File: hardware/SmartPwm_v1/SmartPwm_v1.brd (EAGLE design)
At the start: 154.6 x 198.1 mm, 42 parts, among them IC1 7805T, J1 ESP32-PICO-KIT, Q1 IRF3704-H, Q2 IRF3704-H, Q3 IRF3704-H, Q4 IRF3704-H, U1 ICL7667CBAZA, U3 ICL7667CBAZA

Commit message: remove 1 knob, add 3 individual leds, start component placment
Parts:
- removed MT5: PEC11R-4215F-S0024, PEC11R-4215F-S0024:XDCR_PEC11R-4215F-S0024
- moved SV4 410.4 mm to (96.5, 53.3), turned to 90 degrees
- moved SV3 401.5 mm to (90.2, 53.3), turned to 90 degrees
- moved SV5 387.5 mm to (88.9, 21.6), turned to 90 degrees
- moved C1 359.8 mm to (74.9, 11.4)
- moved U$6 357.4 mm to (77.5, 30.5), turned to 90 degrees
- moved U$8 341.5 mm to (66.0, 5.08)
- moved U3 331.6 mm to (34.3, 62.2)
- moved R8 319.9 mm to (82.5, 8.89), turned to 270 degrees
- moved R6 316.3 mm to (82.5, 12.7)
- moved R9 314.2 mm to (69.8, 11.4), turned to 180 degrees
- moved R7 313.9 mm to (78.7, 8.89), turned to 270 degrees
- moved R10 313.4 mm to (64.8, 11.4), turned to 180 degrees
- moved C10 304.5 mm to (34.3, 71.1), turned to 180 degrees
- moved C12 299.1 mm to (34.3, 67.3), turned to 180 degrees
- moved U$7 297.5 mm to (96.5, 21.6), turned to 270 degrees
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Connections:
- net LDAT3V3 renamed LDAT1_3V3
- removed net K5_A: J1.J3_9, MT5.A
- removed net K5_B: J1.J3_6, MT5.B
- removed net K5_S: J1.J2_17, MT5.2
- removed net LDAT5V: SV2.2, SV2.3, SV3.2, SV3.3, SV4.2, SV4.3, SV5.2, SV5.3, U$6.3
- new net LDAT1_5V: SV1.2, SV1.3, U$6.3
- new net LDAT2_3V3: J1.J2_7, U$6.5
- new net LDAT2_5V: SV2.2, SV2.3, U$6.6
- new net LDAT3_3V3: J1.J3_6, U$6.9
- new net LDAT3_5V: SV3.2, SV3.3, U$6.8
- new net LDAT4_3V3: J1.J3_9, U$6.12
- new net LDAT4_5V: SV4.2, SV4.3, U$6.11
- net GND: now also U$6.13, U$6.4; no longer MT5.1, MT5.COM, MT5.S1, MT5.S2, U$6.5, U$6.9
- net SCL: now also SV5.4; no longer SV1.4
- net SDA: now also SV5.3; no longer SV1.3
- net VCC: no longer U$6.12, U$6.13, U$6.4
- net VDD: now also SV1.4; no longer SV5.4
- net VEE: now also SV5.2; no longer SV1.2
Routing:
- net LOAD_RET4: track 0.00 -> 87.8 mm
- net LOAD_RET3: track 0.00 -> 63.7 mm
- net LOAD_RET2: track 0.00 -> 42.9 mm
- net SCL: track 0.00 -> 38.0 mm
- net VEE: track 0.00 -> 37.2 mm
- net SDA: track 0.00 -> 30.0 mm
- net LOAD_RET1: track 0.00 -> 18.7 mm
- net VDD: track 0.00 -> 11.7 mm
- net TDAT: track 0.00 -> 10.1 mm
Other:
- board size 154.6 x 198.1 mm -> 101.6 x 76.2 mm
- board text added: "7667"
- board text added: "G D D V"
- board text added: "G V D C"

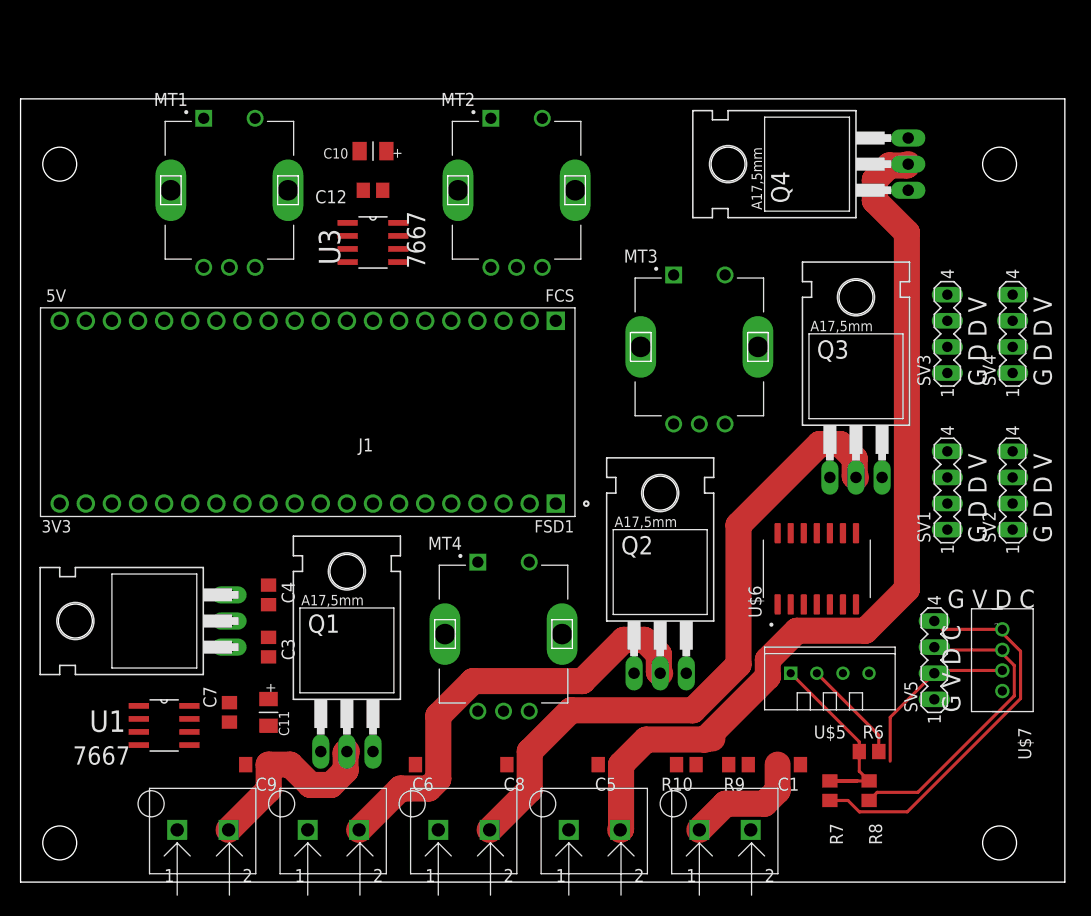
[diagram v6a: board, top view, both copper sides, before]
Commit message: redo placment for more efficient routing
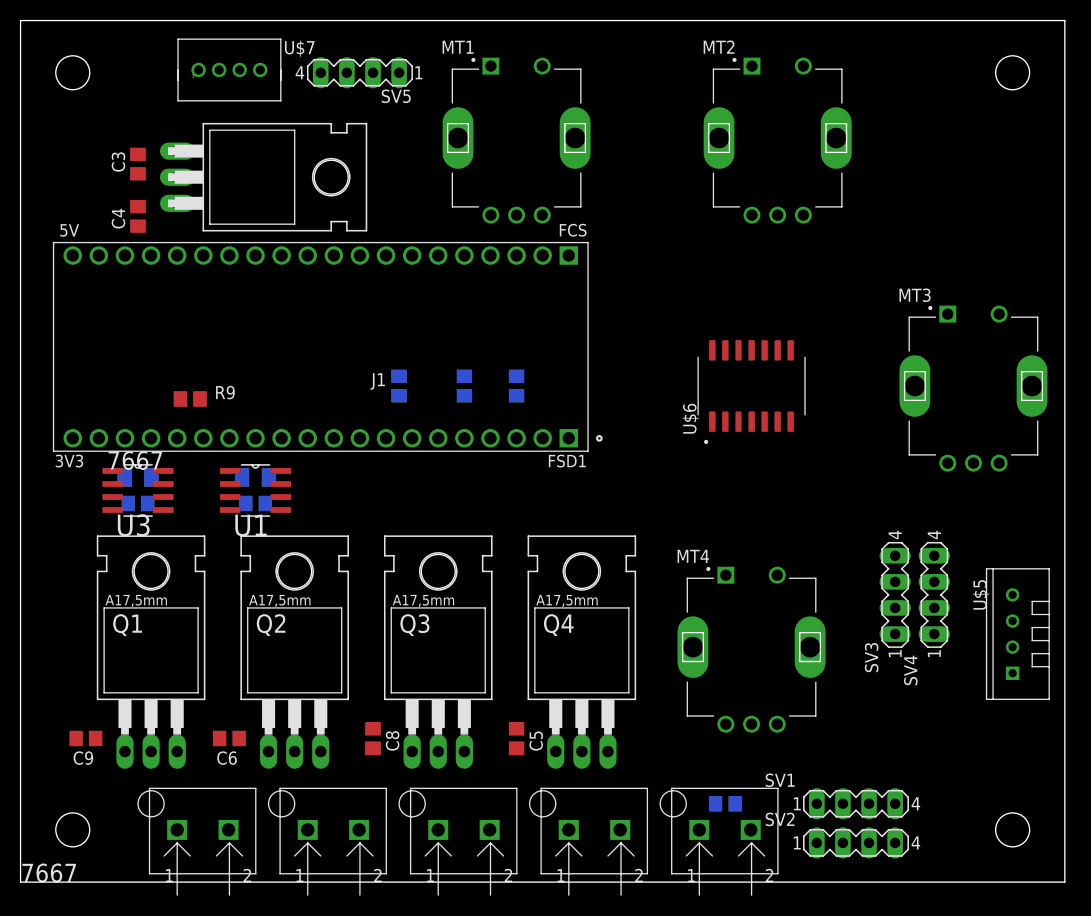
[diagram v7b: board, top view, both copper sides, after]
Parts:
- moved U$7 96.0 mm to (20.3, 80.0), turned to 0 degrees
- moved SV5 79.9 mm to (33.0, 78.7), turned to 180 degrees
- moved R9 64.1 mm to (16.5, 47.0)
- moved R10 59.9 mm to (16.5, 47.0), flipped to the bottom
- moved R6 57.9 mm to (36.8, 48.3), flipped to the bottom, turned to 270 degrees
- moved Q4 56.8 mm to (54.6, 19.1), turned to 0 degrees
- moved R7 53.1 mm to (43.2, 48.3), flipped to the bottom
- moved R8 52.2 mm to (48.3, 48.3), flipped to the bottom
- moved C3 48.7 mm to (11.4, 69.8), turned to 270 degrees
- moved Q3 48.6 mm to (40.6, 19.1)
- moved IC1 45.8 mm to (25.4, 68.6), turned to 270 degrees
- moved C4 39.0 mm to (11.4, 64.8), turned to 90 degrees
- moved SV2 37.5 mm to (81.3, 3.81), turned to 0 degrees
- moved Q2 36.4 mm to (26.7, 19.1)
- moved C10 33.7 mm to (22.9, 39.4), flipped to the bottom, turned to 0 degrees
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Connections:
- net CTRL1: now also J1.J2_17; no longer J1.J3_12
- net CTRL2: now also J1.J2_16; no longer J1.J3_13
- net CTRL3: now also J1.J2_14; no longer J1.J3_11
- net CTRL4: now also J1.J2_15; no longer J1.J3_14
- net K4_A: no longer J1.J2_14
- net K4_S: no longer J1.J2_15
- net VDIV: no longer J1.J2_16
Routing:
- net LOAD_RET4: track 87.8 -> 0.00 mm
- net LOAD_RET3: track 63.7 -> 0.00 mm
- net LOAD_RET2: track 42.9 -> 0.00 mm
- net SCL: track 38.0 -> 0.00 mm
- net VEE: track 37.2 -> 0.00 mm
- net SDA: track 30.0 -> 0.00 mm
- net LOAD_RET1: track 18.7 -> 0.00 mm
- net VDD: track 11.7 -> 0.00 mm
- net TDAT: track 10.1 -> 0.00 mm
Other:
- board size 101.6 x 76.2 mm -> 101.6 x 83.8 mm
- board text removed: "G D D V"
- board text removed: "G V D C"

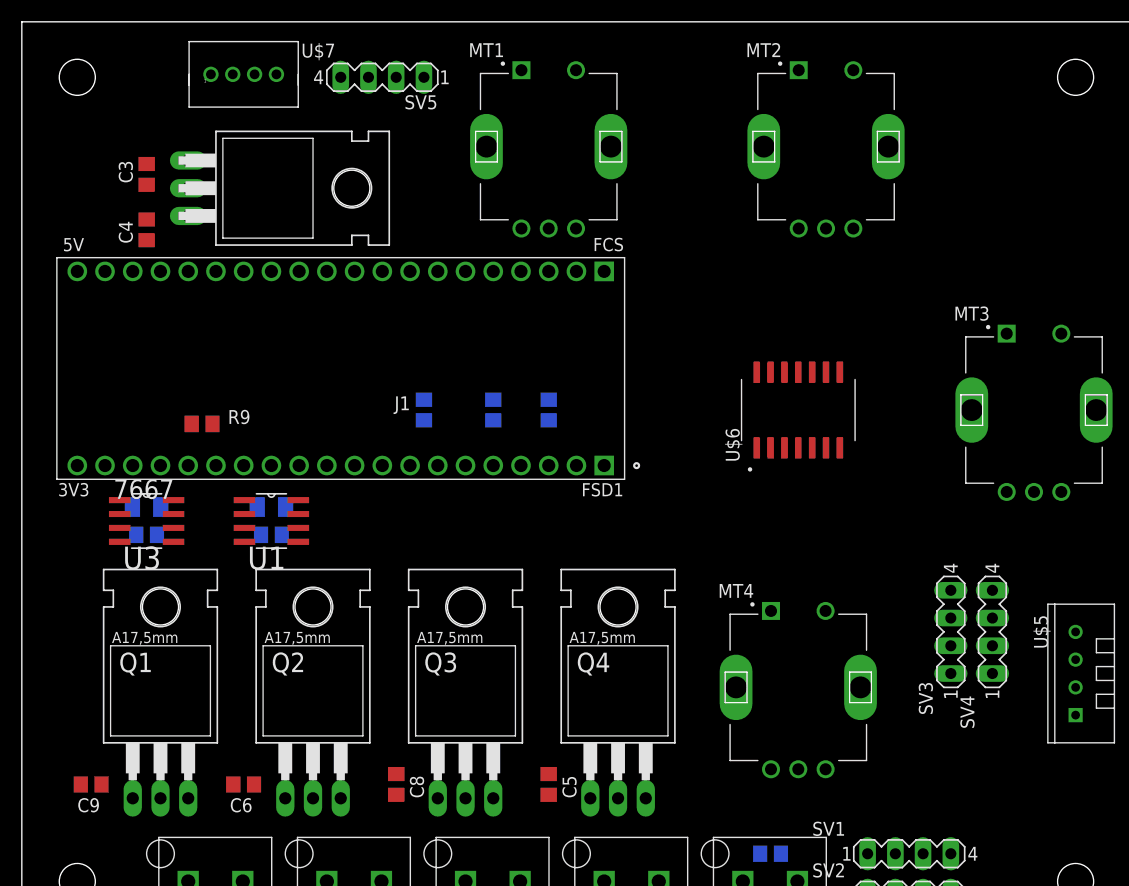
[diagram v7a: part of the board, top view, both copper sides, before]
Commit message: rewire gpios, preliminary routing
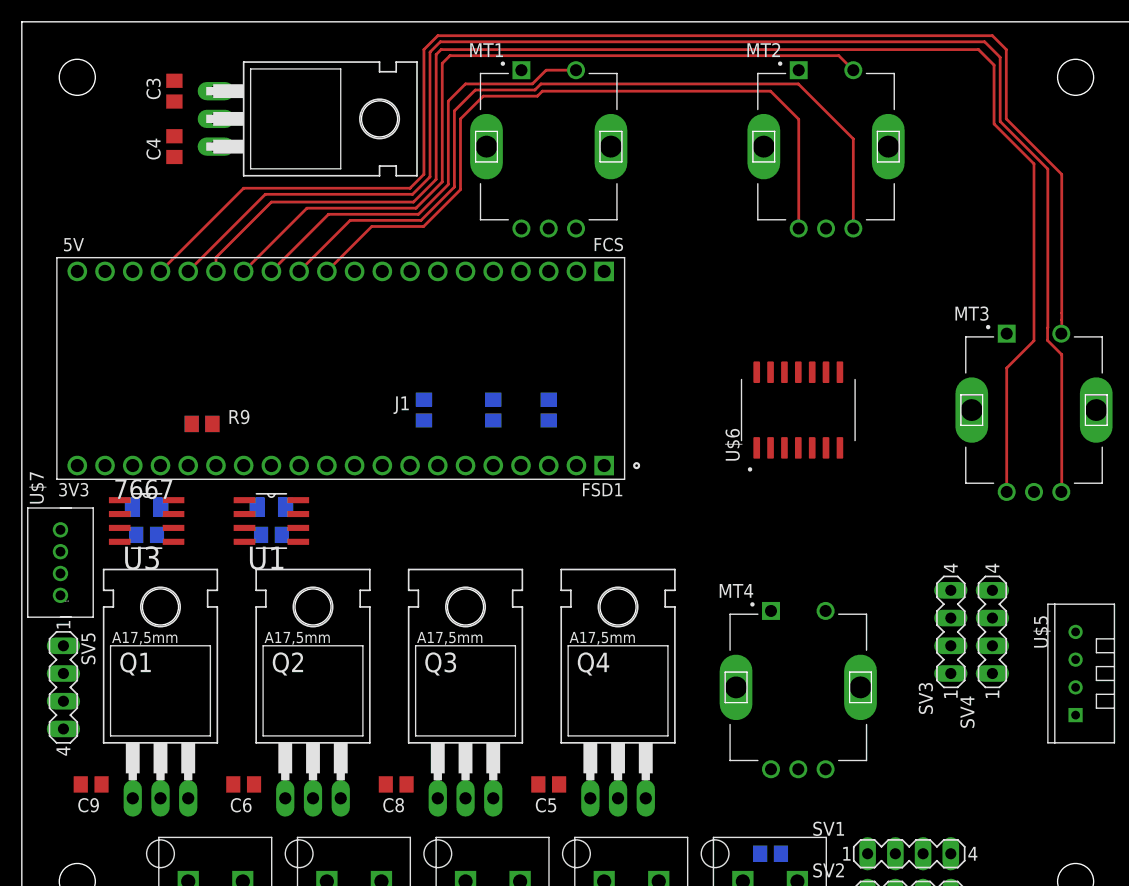
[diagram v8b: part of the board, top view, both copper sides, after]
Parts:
- moved SV5 63.1 mm to (3.81, 22.9), turned to 270 degrees
- moved U$7 49.1 mm to (2.54, 34.3), turned to 90 degrees
- moved C3 8.03 mm to (14.0, 77.5)
- moved C4 8.03 mm to (14.0, 72.4)
- moved IC1 6.84 mm to (27.9, 74.9)
- turned C5 to 0 degrees
- turned C8 to 0 degrees
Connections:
- net K4_A renamed K4A
- net K4_B renamed K4B
- net K4_S renamed K4S
- removed net K1_A: J1.J3_15, MT1.A
- removed net K1_B: J1.J2_9, MT1.B
- removed net K1_S: J1.J3_17, MT1.2
- removed net K2_A: J1.J3_7, MT2.A
- removed net K2_B: J1.J2_10, MT2.B
- removed net K2_S: J1.J3_16, MT2.2
- removed net K3_A: J1.J3_8, MT3.A
- removed net K3_B: J1.J2_11, MT3.B
- removed net K3_S: J1.J3_10, MT3.2
- new net K1A: MT1.A
- new net K1B: MT1.B
- new net K1S: J1.J3_13, MT1.2
- new net K2A: J1.J3_11, MT2.A
- new net K2B: J1.J3_12, MT2.B
- new net K2S: J1.J3_14, MT2.2
- new net K3A: J1.J3_15, MT3.A
- new net K3B: J1.J3_16, MT3.B
- new net K3S: J1.J3_17, MT3.2
- net LDAT1_3V3: now also J1.J2_11; no longer J1.J2_6
- net LDAT2_3V3: now also J1.J2_10; no longer J1.J2_7
- net LDAT3_3V3: now also J1.J2_9; no longer J1.J3_6
- net LDAT4_3V3: now also J1.J2_8; no longer J1.J3_9
- net SCL: no longer J1.J2_5
- net SDA: no longer J1.J2_4
- net TDAT: no longer J1.J2_8
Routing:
- net K3B: track 0.00 -> 132.6 mm
- net K3A: track 0.00 -> 129.4 mm
- net K3S: track 0.00 -> 121.8 mm
- net K2B: track 0.00 -> 72.2 mm
- net K2S: track 0.00 -> 70.9 mm
- net K2A: track 0.00 -> 64.9 mm
- net K1S: track 0.00 -> 40.0 mm
